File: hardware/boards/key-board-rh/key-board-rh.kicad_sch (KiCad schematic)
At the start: 27 parts

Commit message: KiCad sheets are the source of truth (ADR 0019): key-board circuits and boards migrated
- The circuit sheets key-register, key-switch-network and
  key-marker-and-bits own their connections and part facts (fields Row,
  Pins, Pins_source, Note; ports as hierarchical labels). Their
  netlist.yaml is now EXPORTED by tools/kicad.py.
- key-board-rh and key-board-lh are KiCad projects placing those sheets
  once per instance (register, one per key, one per free bit); their
  board-netlist.yaml is exported, with KiCad's ERC over the hierarchy.
- Proved: every exported circuit netlist equals the hand-written one it
  replaces, part by part and net by net; both KiCad boards equal the
  boards the retired tools/board.py assembled. ERC clean.
- key-marker-and-bits is now one free-bit pull-up, replicated 3; marker
  straps are board wiring. nets.yaml gains FREE_BIT.
- tools/kicad.py check: stale exports, stale or edited renders
  (hardware/SHEETS.csv), board ERC, and board wiring vs allocation.yaml vs
  the page table vs key-layout.yaml. Tested: an unexported edit and a
  swapped key both fail.
- CLAUDE.md, hardware/README.md, repo-maintenance.md and tooling.md say
  what is source and what is exported. tools/board.py retired.

Co-Authored-By: Claude Opus 5.5 <noreply@anthropic.com>
Claude-Session: https://claude.ai/code/session_01LmB4muFXnoLprWX4JzuJ5A
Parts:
- removed C-DECOUPLE-165-RH: 100nF, symbol Device:C
- removed C-KEY-RH1, C-KEY-RH2, C-KEY-RH3, C-KEY-RH4, C-KEY-RH5, C-KEY-RH6: 47nF, symbol Device:C
- removed R-KEY-PU-RH1, R-KEY-PU-RH2, R-KEY-PU-RH3, R-KEY-PU-RH4, R-KEY-PU-RH5, R-KEY-PU-RH6: 2k2 1%, symbol Device:R
- removed R-KEY-SER-RH1, R-KEY-SER-RH2, R-KEY-SER-RH3, R-KEY-SER-RH4, R-KEY-SER-RH5, R-KEY-SER-RH6: 100R 1%, symbol Device:R
- removed SW-RH1, SW-RH2, SW-RH3, SW-RH4, SW-RH5, SW-RH6: KS-33, symbol Switch:SW_Push
- removed U-KEYS-RH: 74HC165, symbol 74xx:74HC165
- J-CHAIN: value 12-way FFC ZIF -> 12-way; Note (none) -> right_hand key board. REVERSED: conductor k lands on pin 13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; Pins (none) -> 1=1 2=2 3=3 4=4 5=5 6=6 7=7 8=8 9=9 10=10 11=11 12=12; Row (none) -> J-CHAIN
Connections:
- no-connect marks 3 -> 2
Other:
- added sheet REG (../../cluster/key-register/key-register.kicad_sch)
- added sheet RH1 (../../cluster/key-switch-network/key-switch-network.kicad_sch)
- added sheet RH2 (../../cluster/key-switch-network/key-switch-network.kicad_sch)
- added sheet RH3 (../../cluster/key-switch-network/key-switch-network.kicad_sch)
- added sheet RH4 (../../cluster/key-switch-network/key-switch-network.kicad_sch)
- added sheet RH5 (../../cluster/key-switch-network/key-switch-network.kicad_sch)
- added sheet RH6 (../../cluster/key-switch-network/key-switch-network.kicad_sch)
- note removed: "Every key: R-KEY-PU pulls the register input to 3V3, C-KEY and R-KEY-SER filter it, the switch pulls it to ground. Inputs B and A are the marker straps (0 and 1): tied straight to the rails, no parts. The register's inputs, allocation and marker levels: hardware/cluster/key-marker-and-bits/allocation.yaml."
- title: Right-hand key board (PCB-CLUSTER, right_hand) -> Right-hand key board (right_hand cluster, PCB-CLUSTER)
- moved on the sheet: J-CHAIN

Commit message: First PCB: the left-hand key board, placed from the body CAD and routed
- tools/pcb.py: a board's first layout from its KiCad sheets (netlist,
  footprints) and the body CAD's new exports (key-board outline DXF,
  switch and ribbon-connector positions); then the .kicad_pcb is source.
  check = KiCad DRC with schematic parity + switches where the CAD puts
  them; render = 3D both sides, 2D copper, and fab/ (Gerbers, drill,
  placement), ledgered in hardware/SHEETS.csv. tools/kicad.py check runs it.
- tools/pcb_route.py: a small two-layer grid router for simple boards;
  ground routed as a net plus pours and stitching vias.
- key-board-lh: 24 parts, all nets routed; KiCad DRC 0 errors, schematic
  parity clean (one stock-footprint silkscreen warning). Tested: a switch
  moved 1 mm fails the check.
- Footprints on the sheets; hardware/lib/woody.pretty holds the KS-33
  footprint (marbastlib, banked) with Gateron's STEP lifted by
  switch.pcb_below_seat. J-CHAIN's stand-in is Molex 200528-0120.
- Findings, recorded in tooling.md §4 and DESIGN.md: the ribbon connector
  needs 6.7 mm, the CAD envelope is 5.5; KS-33 pins show only ~0.1 mm
  below a 1.6 mm board (1.2 mm would leave ~0.5).
- setup-env.sh installs footprints, rsvg, shapely and repairs an empty
  global fp-lib-table.

Co-Authored-By: Claude Opus 5.5 <noreply@anthropic.com>
Claude-Session: https://claude.ai/code/session_01LmB4muFXnoLprWX4JzuJ5A
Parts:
- J-CHAIN: footprint (none) -> Connector_FFC-FPC:Molex_200528-0120_1x12-1MP_P1.00mm_Horizontal
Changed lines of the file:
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@@
     (property "Reference" "J-CHAIN" (at 45.72 86.36 0) (effects (font (size 1.27 1.27))))
     (property "Value" "12-way" (at 45.72 119.38 0) (effects (font (size 1.27 1.27))))
-    (property "Footprint" "" (at 45.72 101.6 0) (effects (font (size 1.27 1.27)) hide))
+    (property "Footprint" "Connector_FFC-FPC:Molex_200528-0120_1x12-1MP_P1.00mm_Horizontal" (at 45.72 101.6 0) (effects (font (size 1.27 1.27)) hide))
     (property "Datasheet" "" (at 45.72 101.6 0) (effects (font (size 1.27 1.27)) hide))
     (property "Row" "J-CHAIN" (at 45.72 101.6 0) (effects (font (size 1.27 1.27)) hide))

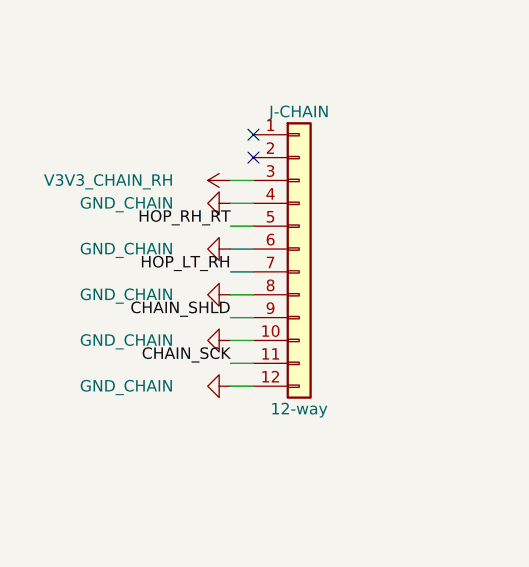
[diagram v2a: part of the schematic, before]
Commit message: Key chain on through-hole 1.27 mm IDC: model, key boards, router fix
The owner's choice (option 2): a right-angle 2x6 1.27 mm shrouded IDC header
on each board (Samtec SHF-106-01-L-D-RA stand-in), the key board's hanging
over the main board's, and a flat IDC ribbon long enough to plug in with the
lid laid beside the body - closed, a flat hairpin along the body, clear of
the LED strip.

- CAD: chain headers, plugs and the hairpin ribbon replace the ZIF/FFC C;
  positions found clear of every switch's pole and pins and the regulator
  block; ribbon length derived from the service position (drc.echo); a plate
  window over the key header's pin tails. body.yaml boards.chain_* and
  routing.chain_* replace ffc_*. 0 DRC FAILs, 0 clashes over 134 solids.
- Key boards: J-CHAIN footprint woody:IDC-Header_2x06_P1.27mm_Samtec_SHF_
  Horizontal (new); pinout moved one pin for the upside-down header (main
  pin n -> key pin 12-n odd / 14-n even); ERC clean. The interface netlist
  follows and agrees pin for pin.
- pcb.py places J-CHAIN from the CAD's "chain" line and checks it; the
  router no longer walls a plated pad off from its own track (1.27 mm pads).
  LH board: DRC 0 errors, parity clean; renders and fab/ regenerated.

The BOM rows, the key-chain page and the ADR 0017 amendment follow in the
next commit.

Co-Authored-By: Claude Opus 5.5 <noreply@anthropic.com>
Claude-Session: https://claude.ai/code/session_01LmB4muFXnoLprWX4JzuJ5A
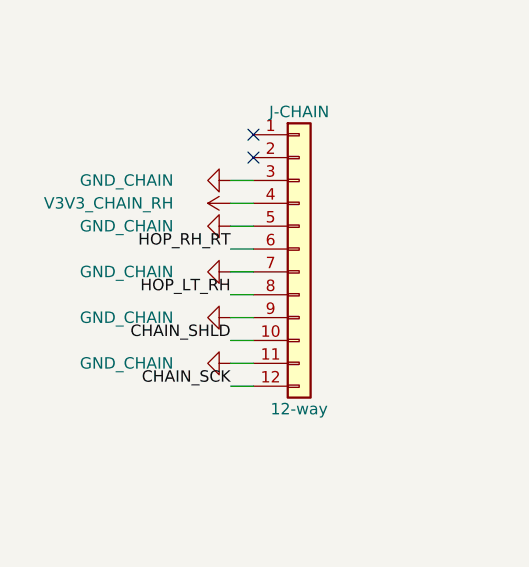
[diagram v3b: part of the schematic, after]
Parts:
- J-CHAIN: footprint Connector_FFC-FPC:Molex_200528-0120_1x12-1MP_P1.00mm_Horizontal -> woody:IDC-Header_2x06_P1.27mm_Samtec_SHF_Horizontal; Note right_hand key board. REVERSED: conductor k lands on pin 13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 -> key-board end of the chain ribbon: 1.27 mm IDC, right-angle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
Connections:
- net CHAIN_SCK: now also J-CHAIN.12 (Pin_12); no longer J-CHAIN.11 (Pin_11)
- net CHAIN_SHLD: now also J-CHAIN.10 (Pin_10); no longer J-CHAIN.9 (Pin_9)
- net GND_CHAIN: now also J-CHAIN.11 (Pin_11), J-CHAIN.3 (Pin_3), J-CHAIN.5 (Pin_5), J-CHAIN.7 (Pin_7), J-CHAIN.9 (Pin_9); no longer J-CHAIN.10 (Pin_10), J-CHAIN.12 (Pin_12), J-CHAIN.4 (Pin_4), J-CHAIN.6 (Pin_6), J-CHAIN.8 (Pin_8)
- net HOP_LT_RH: now also J-CHAIN.8 (Pin_8); no longer J-CHAIN.7 (Pin_7)
- net HOP_RH_RT: now also J-CHAIN.6 (Pin_6); no longer J-CHAIN.5 (Pin_5)
- net V3V3_CHAIN_RH: now also J-CHAIN.4 (Pin_4); no longer J-CHAIN.3 (Pin_3)

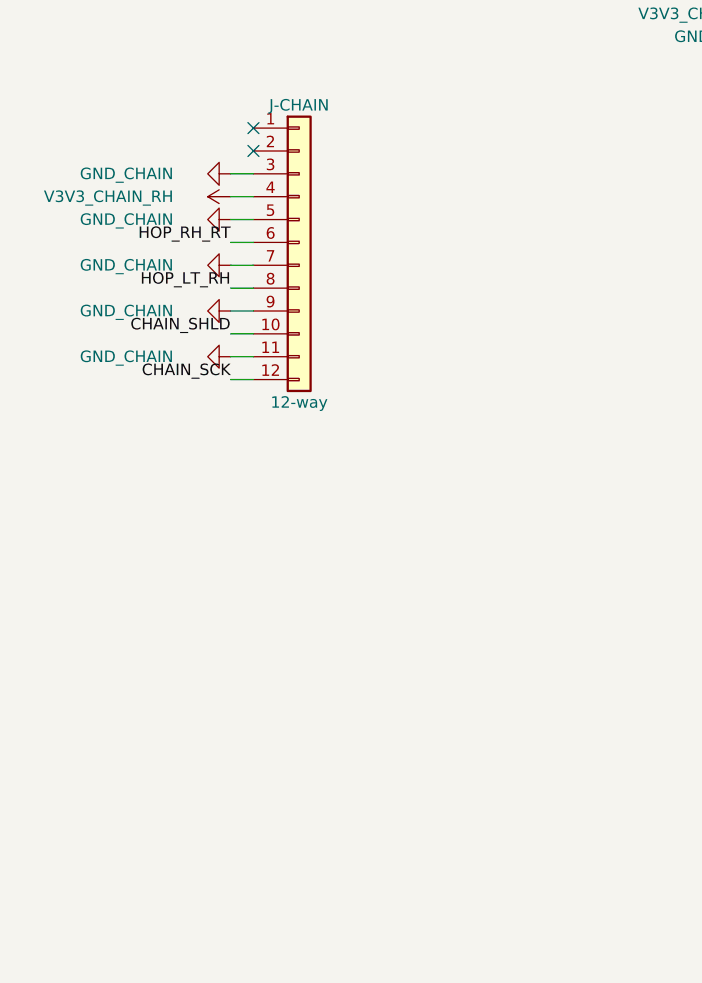
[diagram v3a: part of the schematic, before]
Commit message: LH key board as the worked example: orderable, labelled, testable
- Samtec full prints banked (SHF header, FFSD cable); the header's true
  dimensions replace the catalogue estimates (body.yaml boards.chain_*), and
  the cable is ordered -RN2 (notch reversed on the key-board end): both
  sockets' cables leave downward, the ribbon runs flat, and key-board pin =
  13 - main-board pin. The same-day 12-n/14-n map was wrong and is undone in
  the sheets, the interface netlist and the docs (history in notes.md).
- Model: the hairpin's legs follow the cable's real exit - the main board's
  on the board, clear of the thumb switches' poles; 0 DRC FAILs, 0 clashes.
- Sheets: Manufacturer/MPN/LCSC/Assembly fields from JLC's parts API (JLC
  and LCSC pages banked in datasheets/fab and the manifest); five bring-up
  test pads per key board (TP-CHAIN, copper only).
- pcb.py: JLC's limits in the DRC (layout.yaml fab:), which grew the vias
  and J-CHAIN's pads to the 0.18 mm ring; HASL lead-free in the stackup and
  Gerber job; a generated parts-side silkscreen; the JLC BOM, CPL and
  hand-assembly list in fab/, ledgered against board and sheets.
- Router: a real rip-up (blockers removed too); plated holes no longer wall
  off their own pads.
- hardware/boards/key-board-lh/README.md: sources, ordering, hand assembly,
  bring-up, open items. tooling.md and lib README follow.
All checks pass: CAD, DRC (0/0), KiCad, staleness, BOM, netlist, datasheets.

Co-Authored-By: Claude Opus 5.5 <noreply@anthropic.com>
Claude-Session: https://claude.ai/code/session_01LmB4muFXnoLprWX4JzuJ5A
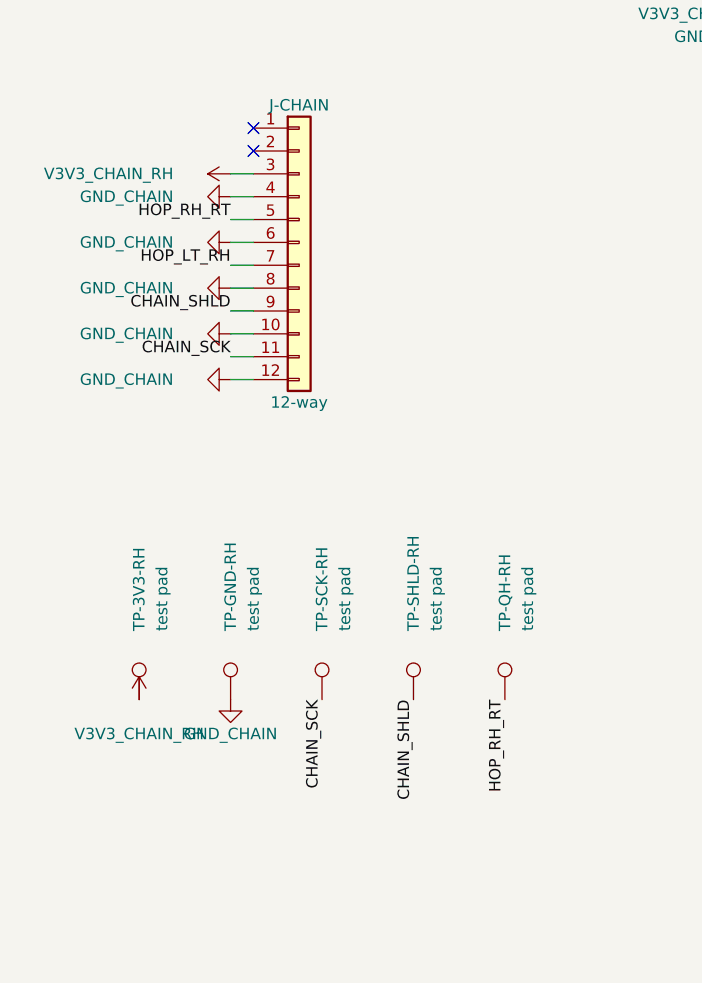
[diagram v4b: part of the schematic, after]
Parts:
- added TP-3V3-RH, TP-GND-RH, TP-QH-RH, TP-SCK-RH, TP-SHLD-RH: test pad, TestPoint:TestPoint_Pad_D1.0mm, symbol Connector:TestPoint
- J-CHAIN: Assembly (none) -> hand; MPN (none) -> SHF-106-01-L-D-RA; Manufacturer (none) -> Samtec; Note key-board end of the chain ribbon: 1.27 mm IDC, right-angle, upside down on the underside, so main-board pin n arrives at pin 12-n (n odd) or 14-n (n even) - key-chain-loom.md, ADR 0017 amended -> key-board end of the chain ribbon: 1.27 mm IDC, right-angle, upside down on the underside; the cable's key-board socket has its notch reversed (FFSD -RN2), so main-board pin n arrives at pin 13-n - key-chain-loom.md
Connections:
- net CHAIN_SCK: now also J-CHAIN.11 (Pin_11), TP-SCK-RH.1; no longer J-CHAIN.12 (Pin_12)
- net CHAIN_SHLD: now also J-CHAIN.9 (Pin_9), TP-SHLD-RH.1; no longer J-CHAIN.10 (Pin_10)
- net GND_CHAIN: now also J-CHAIN.10 (Pin_10), J-CHAIN.12 (Pin_12), J-CHAIN.4 (Pin_4), J-CHAIN.6 (Pin_6), J-CHAIN.8 (Pin_8), TP-GND-RH.1; no longer J-CHAIN.11 (Pin_11), J-CHAIN.3 (Pin_3), J-CHAIN.5 (Pin_5), J-CHAIN.7 (Pin_7), J-CHAIN.9 (Pin_9)
- net HOP_LT_RH: now also J-CHAIN.7 (Pin_7); no longer J-CHAIN.8 (Pin_8)
- net HOP_RH_RT: now also J-CHAIN.5 (Pin_5), TP-QH-RH.1; no longer J-CHAIN.6 (Pin_6)
- net V3V3_CHAIN_RH: now also J-CHAIN.3 (Pin_3), TP-3V3-RH.1; no longer J-CHAIN.4 (Pin_4)

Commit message: WIP: layout-side fixes (networks as T, via-in-pad, segment merge, silk, stackup, TP-SER, drills)
Co-Authored-By: Claude Opus 5.5 <noreply@anthropic.com>
Claude-Session: https://claude.ai/code/session_01LmB4muFXnoLprWX4JzuJ5A
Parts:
- added TP-SER-RH: test pad, TestPoint:TestPoint_Pad_D1.0mm, symbol Connector:TestPoint
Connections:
- net HOP_LT_RH: now also TP-SER-RH.1
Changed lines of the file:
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@@
   )
   (label "HOP_RH_RT" (at 68.58 152.4 270) (fields_autoplaced) (effects (font (size 1.27 1.27)) (justify right bottom)))
+  (symbol (lib_id "Connector:TestPoint") (at 78.74 152.4 0) (unit 1)
+    (in_bom no) (on_board yes) (dnp no)
+    (property "Reference" "TP-SER-RH" (at 78.74 144.78 90) (effects (font (size 1.27 1.27)) (justify left)))
+    (property "Value" "test pad" (at 81.28 144.78 90) (effects (font (size 1.27 1.27)) (justify left)))
+    (property "Footprint" "TestPoint:TestPoint_Pad_D1.0mm" (at 78.74 152.4 0) (effects (font (size 1.27 1.27)) hide))
+    (property "Datasheet" "" (at 78.74 152.4 0) (effects (font (size 1.27 1.27)) hide))
+    (property "Row" "TP-CHAIN" (at 78.74 152.4 0) (effects (font (size 1.27 1.27)) hide))
+    (property "Pins" "1=1" (at 78.74 152.4 0) (effects (font (size 1.27 1.27)) hide))
+    (property "Note" "bring-up test pad: this board's serial input (SER), driven by the next board up the chain - tie it to TP-GND or TP-3V3 on the bench, where nothing drives it (hardware/boards/key-board-rh/README.md)" (at 78.74 152.4 0) (effects (font (size 1.27 1.27)) hide))
+    (property "Assembly" "none" (at 78.74 152.4 0) (effects (font (size 1.27 1.27)) hide))
+    (pin "1")
+    (instances (project "key-board-rh" (path "/0d798814-7e94-52b0-a143-b50dd4dde890" (reference "TP-SER-RH") (unit 1))))
+  )
+  (label "HOP_LT_RH" (at 78.74 152.4 270) (fields_autoplaced) (effects (font (size 1.27 1.27)) (justify right bottom)))
   (sheet_instances (path "/" (page "1")))
 )

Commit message: Key boards: a do-not-fit bulk capacitor footprint; decoupler across the register's supply pins
- C-BULK-CHAIN-LH/-RH: a 10uF 0805 footprint on each key board's 3V3,
  dnp and out of every order, fitted at bring-up only if the FB-CHAIN /
  C-DECOUPLE-165 LC rings (K1-13). New row C-BULK-CHAIN beside FB-CHAIN.
- pcb.py carries the symbol's "Do not populate" and "Exclude from BOM"
  to the footprint, so a dnp part passes schematic parity.
- C-DECOUPLE-165-LH lies across the ends of U-KEYS pins 16 and 15, each a
  2.25 mm stub (K3-8's loop closed through the plane 12.9 mm away), and
  ground now routes to every pin without leaning on the pour.

Co-Authored-By: Claude Opus 5.5 <noreply@anthropic.com>
Claude-Session: https://claude.ai/code/session_01LmB4muFXnoLprWX4JzuJ5A
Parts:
- added C-BULK-CHAIN-RH: 10uF DNP, Capacitor_SMD:C_0805_2012Metric, symbol Device:C
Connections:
- net GND_CHAIN: now also C-BULK-CHAIN-RH.2
- net V3V3_CHAIN_RH: now also C-BULK-CHAIN-RH.1
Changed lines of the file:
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@@
   )
   (label "HOP_LT_RH" (at 78.74 152.4 270) (fields_autoplaced) (effects (font (size 1.27 1.27)) (justify right bottom)))
+  (symbol (lib_id "Device:C") (at 93.98 152.4 0) (unit 1)
+    (in_bom no) (on_board yes) (dnp yes)
+    (property "Reference" "C-BULK-CHAIN-RH" (at 96.52000000000001 151.13 0) (effects (font (size 1.27 1.27)) (justify left)))
+    (property "Value" "10uF DNP" (at 96.52000000000001 153.67000000000002 0) (effects (font (size 1.27 1.27)) (justify left)))
+    (property "Footprint" "Capacitor_SMD:C_0805_2012Metric" (at 93.98 152.4 0) (effects (font (size 1.27 1.27)) hide))
+    (property "Datasheet" "" (at 93.98 152.4 0) (effects (font (size 1.27 1.27)) hide))
+    (property "Row" "C-BULK-CHAIN" (at 93.98 152.4 0) (effects (font (size 1.27 1.27)) hide))
+    (property "Pins" "1=1 2=2" (at 93.98 152.4 0) (effects (font (size 1.27 1.27)) hide))
+    (property "Note" "DO NOT FIT unless the rail rings: FB-CHAIN and C-DECOUPLE-165 make an LC near 0.5 MHz, half the chain clock. Scope this board's VCC while shifting at bring-up; if it rings, fit a 10uF X5R 0805 here, whose ESR damps it (FB-CHAIN row, key-chain-loom/bom.csv)" (at 93.98 152.4 0) (effects (font (size 1.27 1.27)) hide))
+    (property "Assembly" "none" (at 93.98 152.4 0) (effects (font (size 1.27 1.27)) hide))
+    (pin "1")
+    (pin "2")
+    (instances (project "key-board-rh" (path "/0d798814-7e94-52b0-a143-b50dd4dde890" (reference "C-BULK-CHAIN-RH") (unit 1))))
+  )
+  (symbol (lib_id "power:+3V3") (at 93.98 148.59 0) (unit 1)
+    (in_bom yes) (on_board yes) (dnp no)
+    (property "Reference" "#PWR28" (at 93.98 154.94 0) (effects (font (size 1.27 1.27)) hide))
+    (property "Value" "V3V3_CHAIN_RH" (at 93.98 144.78 0) (effects (font (size 1.27 1.27))))
+    (property "Footprint" "" (at 93.98 148.59 0) (effects (font (size 1.27 1.27)) hide))
+    (property "Datasheet" "" (at 93.98 148.59 0) (effects (font (size 1.27 1.27)) hide))
+    (pin "1")
+    (instances (project "key-board-rh" (path "/0d798814-7e94-52b0-a143-b50dd4dde890" (reference "#PWR28") (unit 1))))
+  )
+  (symbol (lib_id "power:GND") (at 93.98 156.21 0) (unit 1)
+    (in_bom yes) (on_board yes) (dnp no)
+    (property "Reference" "#PWR29" (at 93.98 162.56 0) (effects (font (size 1.27 1.27)) hide))
+    (property "Value" "GND_CHAIN" (at 93.98 160.02 0) (effects (font (size 1.27 1.27))))
+    (property "Footprint" "" (at 93.98 156.21 0) (effects (font (size 1.27 1.27)) hide))
+    (property "Datasheet" "" (at 93.98 156.21 0) (effects (font (size 1.27 1.27)) hide))
+    (pin "1")
+    (instances (project "key-board-rh" (path "/0d798814-7e94-52b0-a143-b50dd4dde890" (reference "#PWR29") (unit 1))))
+  )
   (sheet_instances (path "/" (page "1")))
 )
